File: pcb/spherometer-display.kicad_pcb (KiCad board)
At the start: 2 copper layers, 34 x 14 mm, 14 parts, among them J1 Battery, J2 Indicator, J3 Disp, J4 Programming, Q1 NPN, Q2 NPN, SW1 UI-Button, U1 ATTINY85V-10SU

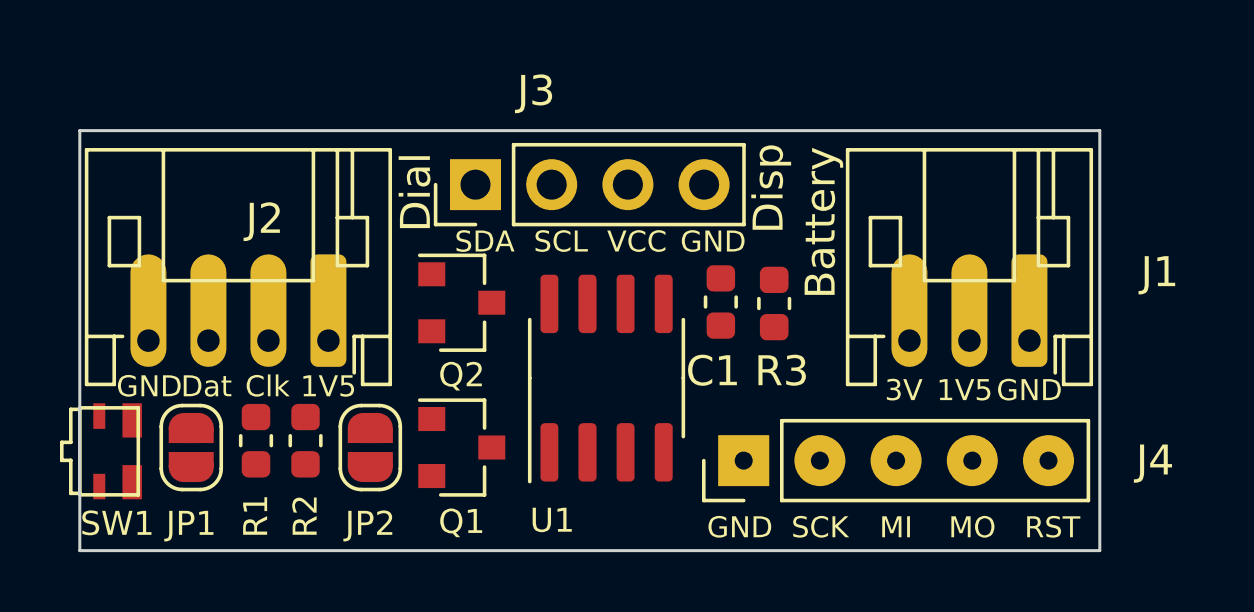
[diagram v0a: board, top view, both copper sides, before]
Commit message: Route board; add Makefile to create fab files.
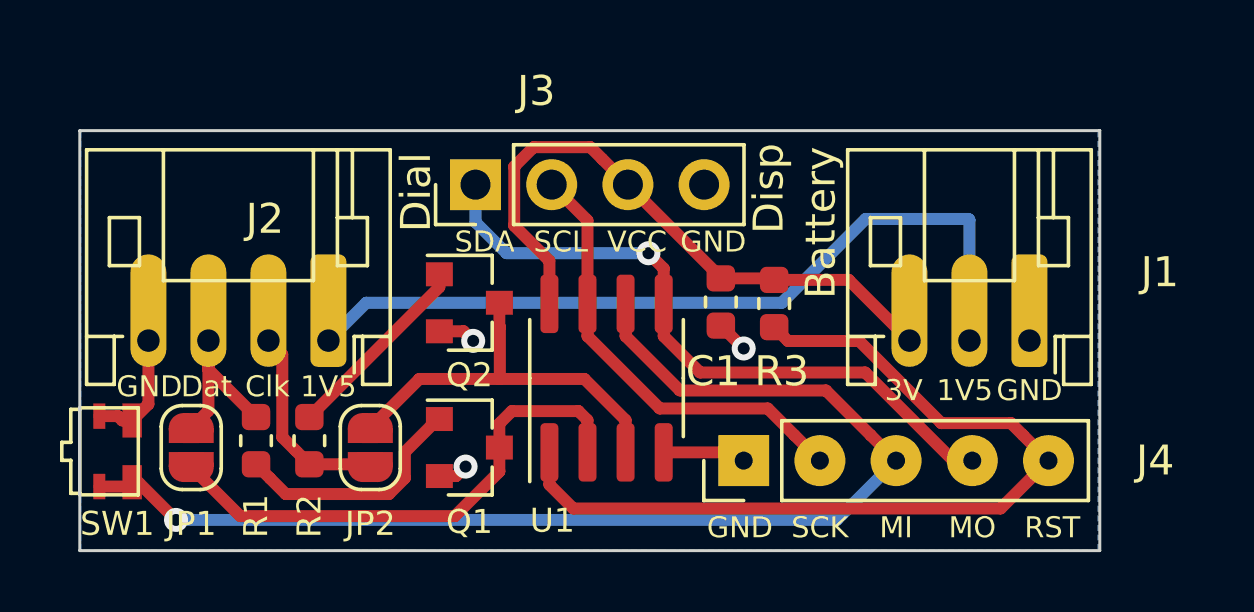
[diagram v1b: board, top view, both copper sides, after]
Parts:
- added REF**: OSHW-Symbol_6.7x6mm_SilkScreen, Symbol:OSHW-Symbol_6.7x6mm_SilkScreen, B.Cu at (82.8, 66.5)
- moved Q1 0.25 mm to (78.5, 67.6)
- moved Q2 0.25 mm to (78.5, 62.7)
- moved R2 0.13 mm to (73.2, 67.3), turned to 270 degrees
- turned JP2 to 90 degrees
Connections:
- SW1 pad 1: /MISO -> GND
- SW1 pad 2: GND -> /MISO
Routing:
- net /MISO: track 0.00 -> 39.8 mm, vias 0 -> 1
- net /Reset: track 0.00 -> 29.7 mm
- net +1V5: track 0.00 -> 27.1 mm
- net /SDA_MOSI: track 0.00 -> 22.4 mm, vias 0 -> 1
- net VCC: track 0.00 -> 21.2 mm
- net Net-(JP1-Pad2): track 0.00 -> 17.5 mm
- net /SCL_SCK: track 0.00 -> 15.0 mm
- net Net-(JP2-Pad2): track 0.00 -> 13.4 mm
- net GND: track 0.00 -> 10.2 mm, vias 0 -> 3
- net Net-(Q1-Pad1): track 0.00 -> 8.07 mm
- net /Clock: track 0.00 -> 6.76 mm
- net Net-(Q2-Pad1): track 0.00 -> 6.56 mm
- net /Data: track 0.00 -> 6.36 mm
- added copper zone on B.Cu, net GND
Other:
- board text added: "%%gitversion%%"
- board text added: "github.com/hzeller/digi-spherometer"
- board text added: "© 2019 CC-BY-SA Henner Zeller"
